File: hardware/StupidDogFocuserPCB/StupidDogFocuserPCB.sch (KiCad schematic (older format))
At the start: 17 parts, among them M1 Stepper_Motor_bipolar, SW1 Rotary_Encoder_Switch, U1 DHT11, U2 SN74HC14N

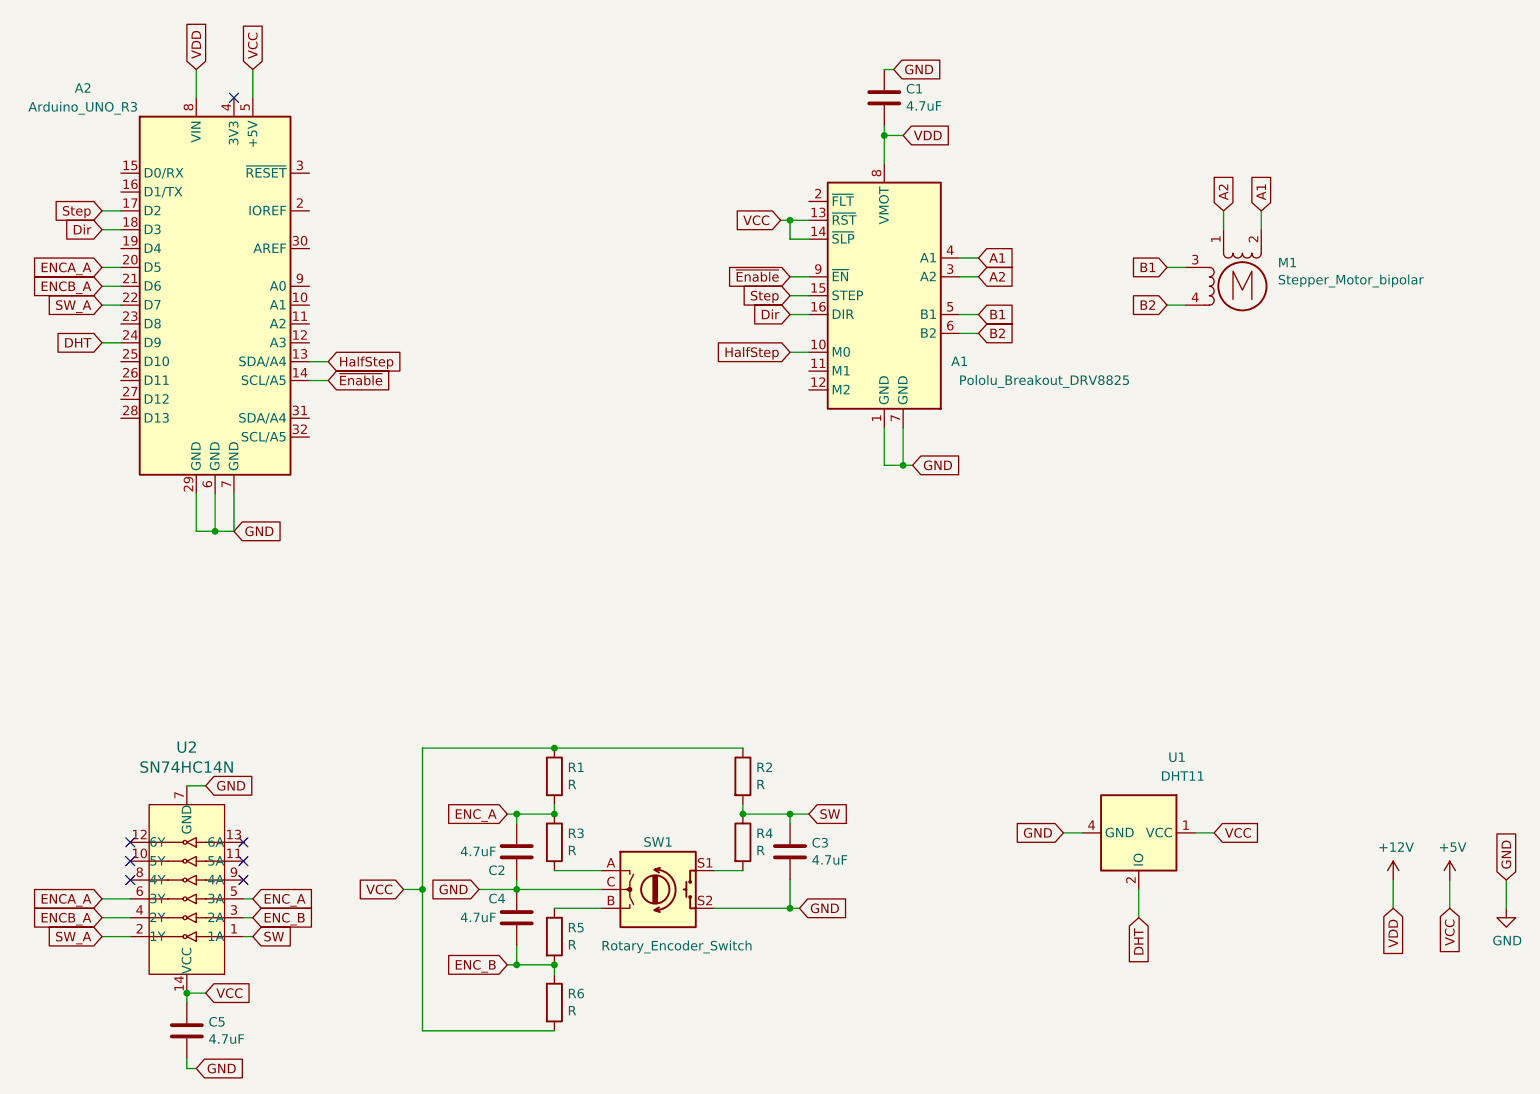
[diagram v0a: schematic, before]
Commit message: Remap/pins (#14)
* Remapped kicad pins. Still need to map firmware.

* no connections added to unused pins.

* moved dht pin.

* moved pins in sketch. Added optimize interrupts flag. Changed error messages.
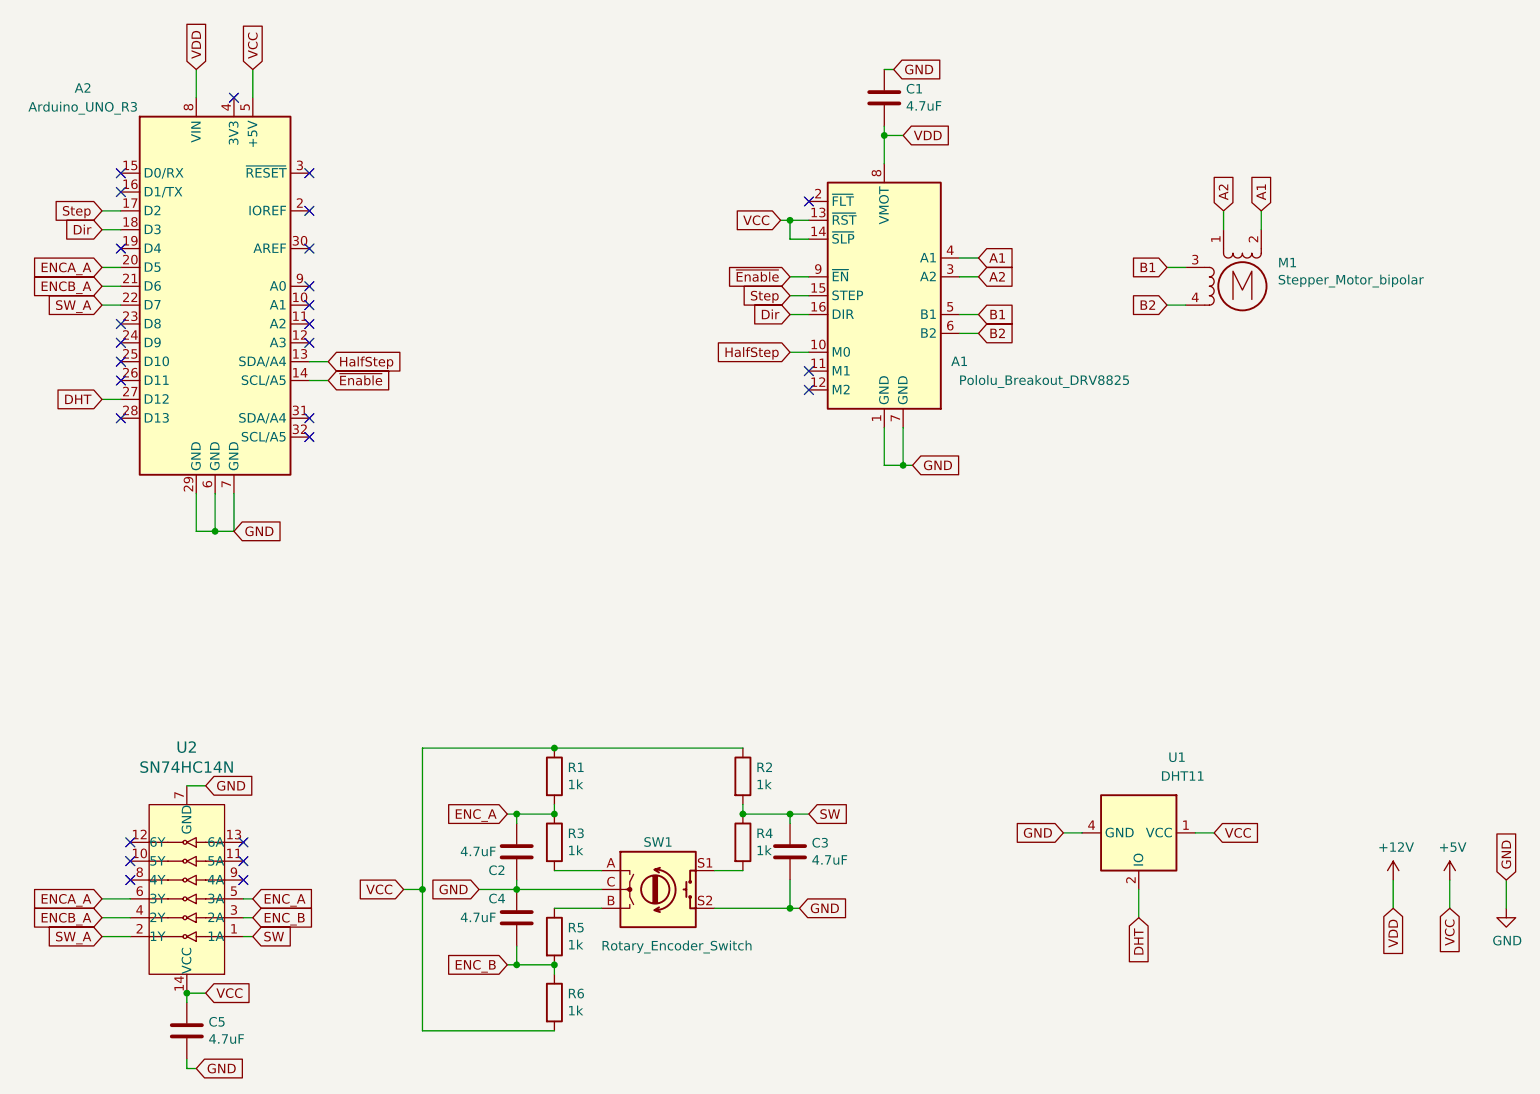
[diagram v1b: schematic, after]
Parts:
- R1, R2, R3, R4, R5, R6: value R -> 1k
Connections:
- net DHT: now also A2.27 (D12); no longer A2.24 (D9)
- no-connect marks 7 -> 27

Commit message: Hardware/cleanup (#22)
* added m1 and m2

* gerbers
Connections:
- net M2: now reaches A2.11 (A2)
- net M2: now also A1.12 (M2)
- net M1: now reaches A2.12 (A3)
- net M1: now also A1.11 (M1)
- net HalfStep renamed M0
- no-connect marks 27 -> 23
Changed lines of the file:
@@
 	5800 2700 5900 2700
 Text GLabel 5800 2700 0    50   Input ~ 0
-HalfStep
+M0
 Wire Wire Line
 	5800 2300 5900 2300
@@
 DHT
 Text GLabel 3350 2750 2    50   Input ~ 0
-HalfStep
+M0
 Text GLabel 2150 2450 0    50   Input ~ 0
 SW_A
@@
 NoConn ~ 3250 2350
 NoConn ~ 3250 2450
-NoConn ~ 3250 2550
-NoConn ~ 3250 2650
 NoConn ~ 3250 3050
 NoConn ~ 3250 3150
@@
 NoConn ~ 2250 1850
 NoConn ~ 2250 1750
-NoConn ~ 5900 2800
-NoConn ~ 5900 2900
 NoConn ~ 5900 1900
 Wire Wire Line
 	2150 2950 2250 2950
 NoConn ~ 2250 3050
+Text GLabel 5800 2800 0    50   Input ~ 0
+M1
+Text GLabel 5800 2900 0    50   Input ~ 0
+M2
+Text GLabel 3350 2650 2    50   Input ~ 0
+M1
+Text GLabel 3350 2550 2    50   Input ~ 0
+M2
+Wire Wire Line
+	3350 2550 3250 2550
+Wire Wire Line
+	3250 2650 3350 2650
+Wire Wire Line
+	5800 2800 5900 2800
+Wire Wire Line
+	5900 2900 5800 2900
 $EndSCHEMATC
